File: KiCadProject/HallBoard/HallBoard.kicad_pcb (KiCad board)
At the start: 2 copper layers, 6 parts, among them J101 JST_SM04B, J102 JST_SM04B, U101 TLE493D

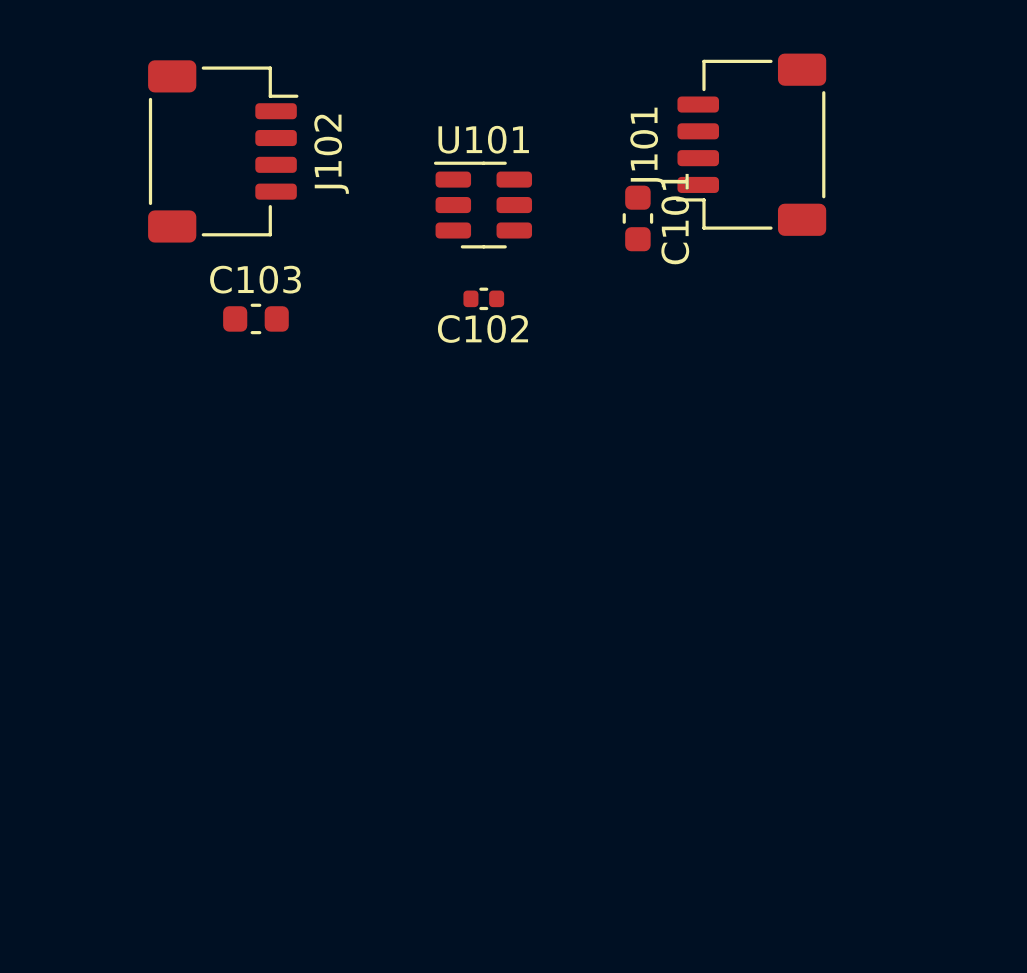
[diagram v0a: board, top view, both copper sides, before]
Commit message: All PCB's should be done. Do a final check before ordering.
Signed-off-by: Eldalote.Electronics <Eldalote.Electronics@gmail.com>
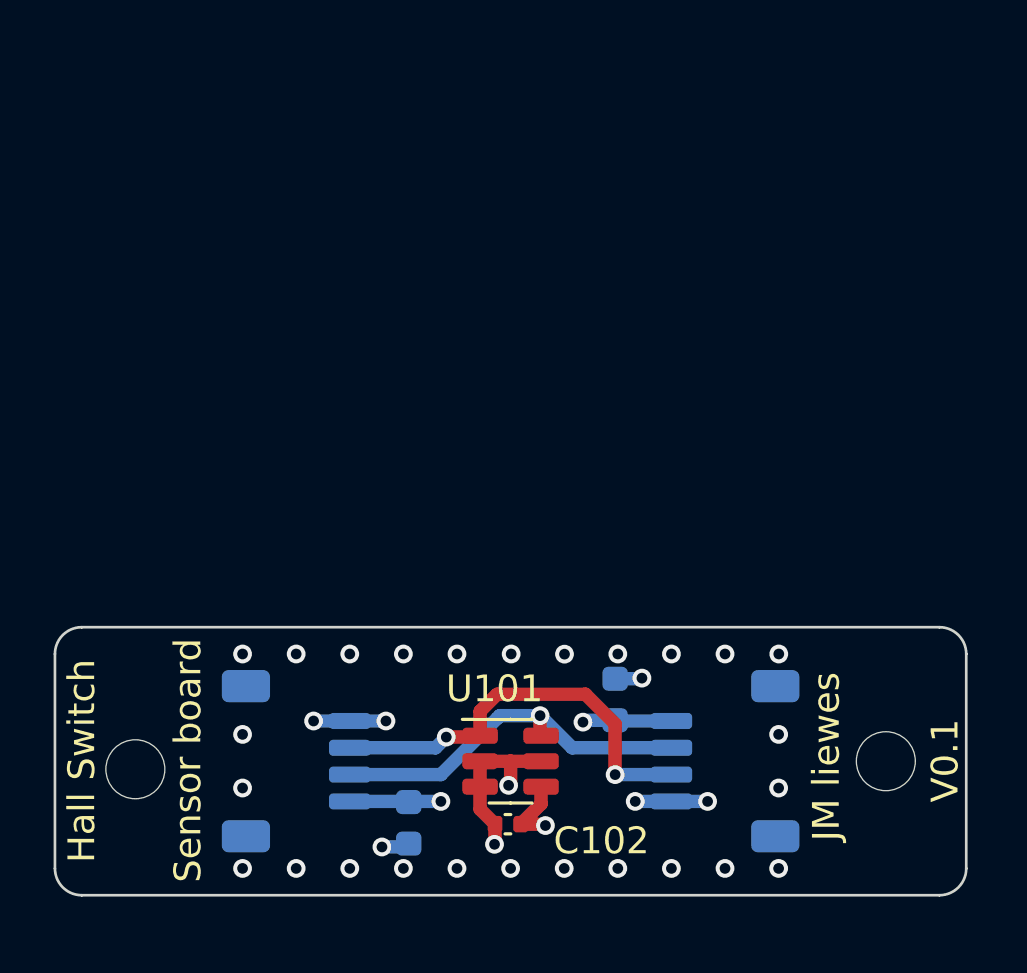
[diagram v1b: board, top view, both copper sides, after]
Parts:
- added REF**: MountingHole_2.2mm_M2, MountingHole:MountingHole_2.2mm_M2, F.Cu at (164.0, 100.0)
- added REF**: MountingHole_2.2mm_M2, MountingHole:MountingHole_2.2mm_M2, F.Cu at (136.0, 100.3)
- C101, C103, J101, J102: moved to B.Cu
- moved C101 24.1 mm to (146.2, 102.3)
- moved J101 23.0 mm to (158.0, 100.0), turned to -90 degrees
- moved J102 22.9 mm to (142.0, 100.0), turned to 90 degrees
- moved U101 20.8 mm to (150.0, 100.0)
- moved C102 19.6 mm to (149.9, 102.3)
- moved C103 19.5 mm to (153.9, 97.7), turned to 90 degrees
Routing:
- net /I2C_SCL: track 0.00 -> 15.7 mm, vias 0 -> 2
- net /I2C_SDA: track 0.00 -> 14.2 mm, vias 0 -> 1
- net GND: track 0.00 -> 14.0 mm, vias 0 -> 34
- net +3V3: track 0.00 -> 9.19 mm, vias 0 -> 3
- added copper zone on In2.Cu, net +3V3
- added copper zone on In1.Cu, net GND
- added copper zone on In3.Cu, net GND
- added copper zone on In4.Cu, net GND
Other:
- board outline added: 34 x 10 mm
- copper layers 2 -> 6
- board text added: "Hall Switch"
- board text added: "JM liewes"
- board text added: "Sensor board"
- board text added: "V0.1"
- board text added: "jlcjlcjlcjlc"

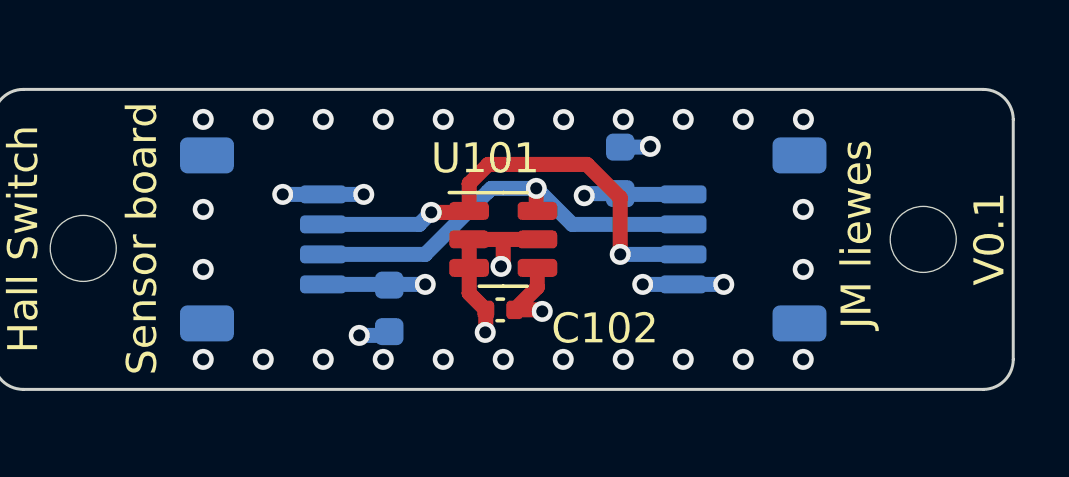
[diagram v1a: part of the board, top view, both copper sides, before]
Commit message: Made ready to order PCBs. Some problems with ordering due to misunderstanding. Thinking about solutions
Signed-off-by: Eldalote.Electronics <Eldalote.Electronics@gmail.com>
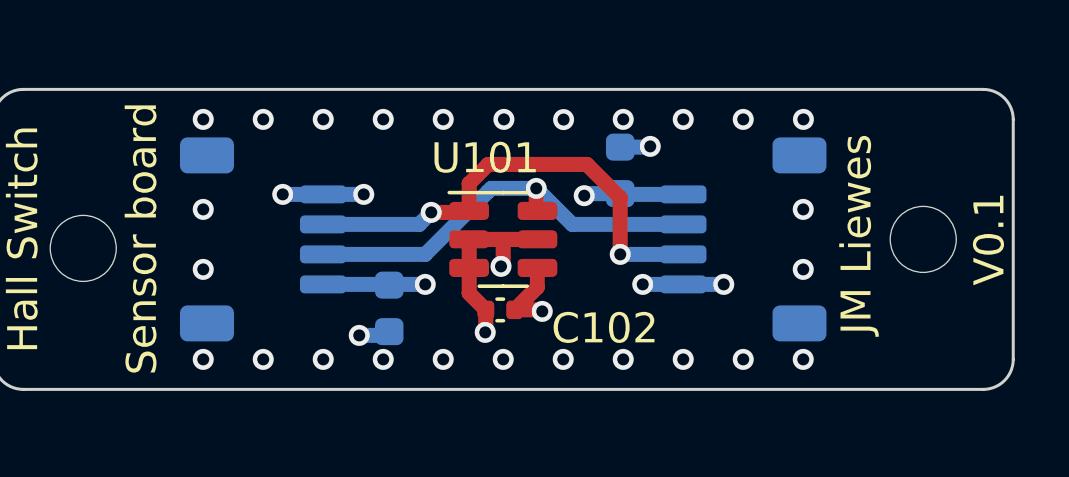
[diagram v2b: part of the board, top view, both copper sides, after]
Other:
- board text added: "JM Liewes"
- board text removed: "JM liewes"
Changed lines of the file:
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@@
       (layerselection 0x00010fc_ffffffff)
       (disableapertmacros false)
-      (usegerberextensions false)
+      (usegerberextensions true)
       (usegerberattributes true)
       (usegerberadvancedattributes true)
@@
       (plotinvisibletext false)
       (sketchpadsonfab false)
-      (subtractmaskfromsilk false)
+      (subtractmaskfromsilk true)
       (outputformat 1)
       (mirror false)
-      (drillshape 1)
+      (drillshape 0)
       (scaleselection 1)
-      (outputdirectory "")
+      (outputdirectory "Fab/")
     )
   )
@@
     (pad "4" smd roundrect (at 1.5 2 90) (size 0.6 1.55) (layers "B.Cu" "B.Paste" "B.Mask") (roundrect_rratio 0.25)
       (net 2 "GND") (pinfunction "Pin_4") (pintype "passive"))
-    (pad "MP" smd roundrect (at -2.8 -1.875 90) (size 1.2 1.8) (layers "B.Cu" "B.Paste" "B.Mask") (roundrect_rratio 0.208333))
-    (pad "MP" smd roundrect (at 2.8 -1.875 90) (size 1.2 1.8) (layers "B.Cu" "B.Paste" "B.Mask") (roundrect_rratio 0.208333))
+    (pad "MP" smd roundrect (at -2.8 -1.875 90) (size 1.2 1.8) (layers "B.Cu" "B.Paste" "B.Mask") (roundrect_rratio 0.2083333333))
+    (pad "MP" smd roundrect (at 2.8 -1.875 90) (size 1.2 1.8) (layers "B.Cu" "B.Paste" "B.Mask") (roundrect_rratio 0.2083333333))
     (model "F:/Engineering/Projects/Divelamp/KiCadImports/3DModels/SM04B-SRSS-TB.STEP"
       (offset (xyz 0 1.5 -0.25))
@@
     (pad "4" smd roundrect (at 1.5 2 270) (size 0.6 1.55) (layers "B.Cu" "B.Paste" "B.Mask") (roundrect_rratio 0.25)
       (net 2 "GND") (pinfunction "Pin_4") (pintype "passive"))
-    (pad "MP" smd roundrect (at -2.8 -1.875 270) (size 1.2 1.8) (layers "B.Cu" "B.Paste" "B.Mask") (roundrect_rratio 0.208333))
-    (pad "MP" smd roundrect (at 2.8 -1.875 270) (size 1.2 1.8) (layers "B.Cu" "B.Paste" "B.Mask") (roundrect_rratio 0.208333))
+    (pad "MP" smd roundrect (at -2.8 -1.875 270) (size 1.2 1.8) (layers "B.Cu" "B.Paste" "B.Mask") (roundrect_rratio 0.2083333333))
+    (pad "MP" smd roundrect (at 2.8 -1.875 270) (size 1.2 1.8) (layers "B.Cu" "B.Paste" "B.Mask") (roundrect_rratio 0.2083333333))
     (model "F:/Engineering/Projects/Divelamp/KiCadImports/3DModels/SM04B-SRSS-TB.STEP"
       (offset (xyz 0 1.5 -0.25))
@@
     (effects (font (size 1 1) (thickness 0.15)) (justify mirror))
   )
-  (gr_text "JM liewes" (at 161.78 99.83 90) (layer "F.SilkS")
+  (gr_text "JM Liewes" (at 161.78 99.83 90) (layer "F.SilkS")
     (effects (font (size 1 1) (thickness 0.16)))
   )

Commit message: Started work on body 3d work
Signed-off-by: Eldalote.Electronics <Eldalote.Electronics@gmail.com>
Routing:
- net +3V3: track 9.19 -> 18.9 mm, vias 3 -> 2
- added copper zone on B.Cu, net GND
- added copper zone on F.Cu, net GND
- removed copper zone on In2.Cu, net +3V3
- removed copper zone on In1.Cu, net GND
- removed copper zone on In3.Cu, net GND
- removed copper zone on In4.Cu, net GND
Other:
- copper layers 6 -> 2
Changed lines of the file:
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@@
   (layers
     (0 "F.Cu" signal)
-    (1 "In1.Cu" signal)
-    (2 "In2.Cu" signal)
-    (3 "In3.Cu" signal)
-    (4 "In4.Cu" signal)
     (31 "B.Cu" signal)
     (32 "B.Adhes" user "B.Adhesive")
@@
       (layer "F.Mask" (type "Top Solder Mask") (thickness 0.01))
       (layer "F.Cu" (type "copper") (thickness 0.035))
-      (layer "dielectric 1" (type "core") (thickness 0.274) (material "FR4") (epsilon_r 4.5) (loss_tangent 0.02))
-      (layer "In1.Cu" (type "copper") (thickness 0.035))
-      (layer "dielectric 2" (type "prepreg") (thickness 0.274) (material "FR4") (epsilon_r 4.5) (loss_tangent 0.02))
-      (layer "In2.Cu" (type "copper") (thickness 0.035))
-      (layer "dielectric 3" (type "core") (thickness 0.274) (material "FR4") (epsilon_r 4.5) (loss_tangent 0.02))
-      (layer "In3.Cu" (type "copper") (thickness 0.035))
-      (layer "dielectric 4" (type "prepreg") (thickness 0.274) (material "FR4") (epsilon_r 4.5) (loss_tangent 0.02))
-      (layer "In4.Cu" (type "copper") (thickness 0.035))
-      (layer "dielectric 5" (type "core") (thickness 0.274) (material "FR4") (epsilon_r 4.5) (loss_tangent 0.02))
+      (layer "dielectric 1" (type "core") (thickness 1.51) (material "FR4") (epsilon_r 4.5) (loss_tangent 0.02))
       (layer "B.Cu" (type "copper") (thickness 0.035))
       (layer "B.Mask" (type "Bottom Solder Mask") (thickness 0.01))
@@
     (effects (font (size 1 1) (thickness 0.15)))
   )
-  (segment (start 150.38 102.35) (end 151.25 102.35) (width 0.5) (layer "F.Cu") (net 1))
-  (segment (start 151.1375 101.5925) (end 150.38 102.35) (width 0.5) (layer "F.Cu") (net 1))
-  (segment (start 151.1375 100.95) (end 151.1375 101.5925) (width 0.5) (layer "F.Cu") (net 1))
-  (segment (start 151.25 102.35) (end 151.3 102.4) (width 0.5) (layer "F.Cu") (net 1))
+  (segment (start 148.2 103.2) (end 150 103.2) (width 0.5) (layer "F.Cu") (net 1))
+  (segment (start 151.85 102.35) (end 150.85 102.35) (width 0.5) (layer "F.Cu") (net 1))
+  (segment (start 150 103.2) (end 150.85 102.35) (width 0.5) (layer "F.Cu") (net 1))
+  (segment (start 150.4 102.33) (end 150.38 102.35) (width 0.5) (layer "F.Cu") (net 1))
+  (segment (start 152.7 101.5) (end 151.85 102.35) (width 0.5) (layer "F.Cu") (net 1))
+  (segment (start 150.38 102.35) (end 150.85 102.35) (width 0.5) (layer "F.Cu") (net 1))
+  (segment (start 147.4 102.4) (end 148.2 103.2) (width 0.5) (layer "F.Cu") (net 1))
+  (segment (start 151.1375 100.95) (end 150.4 101.6875) (width 0.5) (layer "F.Cu") (net 1))
+  (segment (start 147.4 101.5) (end 147.4 102.4) (width 0.5) (layer "F.Cu") (net 1))
+  (segment (start 152.7 98.542453) (end 152.7 101.5) (width 0.5) (layer "F.Cu") (net 1))
+  (segment (start 150.4 101.6875) (end 150.4 102.33) (width 0.5) (layer "F.Cu") (net 1))
   (via (at 147.4 101.5) (size 0.7) (drill 0.4) (layers "F.Cu" "B.Cu") (net 1))
   (via (at 152.7 98.542453) (size 0.7) (drill 0.4) (layers "F.Cu" "B.Cu") (net 1))
-  (via (at 151.3 102.4) (size 0.7) (drill 0.4) (layers "F.Cu" "B.Cu") (net 1))
   (segment (start 152.767453 98.475) (end 153.9 98.475) (width 0.5) (layer "B.Cu") (net 1))
   (segment (start 152.7 98.542453) (end 152.767453 98.475) (width 0.5) (layer "B.Cu") (net 1))
@@
   (segment (start 147.4 101.5) (end 146.25 101.5) (width 0.5) (layer "B.Cu") (net 1))
   (segment (start 148.8625 100) (end 148.8625 100.95) (width 0.5) (layer "F.Cu") (net 2))
+  (segment (start 149.37 102.4) (end 149.42 102.35) (width 0.5) (layer "F.Cu") (net 2))
   (segment (start 148.8625 100) (end 150 100) (width 0.5) (layer "F.Cu") (net 2))
   (segment (start 148.8625 101.7925) (end 149.42 102.35) (width 0.5) (layer "F.Cu") (net 2))
   (segment (start 148.8625 100.95) (end 148.8625 101.7925) (width 0.5) (layer "F.Cu") (net 2))
-  (segment (start 149.42 103.08) (end 149.4 103.1) (width 0.5) (layer "F.Cu") (net 2))
+  (segment (start 148.6 102.4) (end 149.37 102.4) (width 0.5) (layer "F.Cu") (net 2))
   (segment (start 150 100.8255) (end 149.9255 100.9) (width 0.5) (layer "F.Cu") (net 2))
   (segment (start 150 100) (end 151.1375 100) (width 0.5) (layer "F.Cu") (net 2))
   (segment (start 150 100) (end 150 100.8255) (width 0.5) (layer "F.Cu") (net 2))
-  (segment (start 149.42 102.35) (end 149.42 103.08) (width 0.5) (layer "F.Cu") (net 2))
   (via (at 140 101) (size 0.7) (drill 0.4) (layers "F.Cu" "B.Cu") (net 2))
   (via (at 145.2 103.2) (size 0.7) (drill 0.4) (layers "F.Cu" "B.Cu") (net 2))
@@
   (via (at 156 104) (size 0.7) (drill 0.4) (layers "F.Cu" "B.Cu") (net 2))
   (via (at 140 99) (size 0.7) (drill 0.4) (layers "F.Cu" "B.Cu") (net 2))
-  (via (at 149.4 103.1) (size 0.7) (drill 0.4) (layers "F.Cu" "B.Cu") (net 2))
+  (via (at 148.6 102.4) (size 0.7) (drill 0.4) (layers "F.Cu" "B.Cu") (net 2))
   (via (at 152 104) (size 0.7) (drill 0.4) (layers "F.Cu" "B.Cu") (net 2))
   (via (at 152.010917 96.005981) (size 0.7) (drill 0.4) (layers "F.Cu" "B.Cu") (net 2))
@@
   (segment (start 153.9 100.5) (end 156 100.5) (width 0.5) (layer "B.Cu") (net 4))
   (segment (start 144 99.5) (end 147.2 99.5) (width 0.5) (layer "B.Cu") (net 4))
-  (zone (net 2) (net_name "GND") (layers "In1.Cu" "In3.Cu" "In4.Cu") (hatch edge 0.508)
+  (zone (net 2) (net_name "GND") (layers F&B.Cu) (hatch edge 0.508)
     (connect_pads yes (clearance 0.2))
     (min_thickness 0.2) (filled_areas_thickness no)
@@
     (polygon
       (pts
-        (xy 161 106)
-        (xy 139 106)
-        (xy 139 94)
-        (xy 161 94)
+        (xy 161 104.5)
+        (xy 139 104.5)
+        (xy 139 95.5)
+        (xy 161 95.5)
       )
     )
-  )
-  (zone (net 1) (net_name "+3V3") (layer "In2.Cu") (hatch edge 0.508)
-    (connect_pads yes (clearance 0.2))
-    (min_thickness 0.2) (filled_areas_thickness no)
-    (fill yes (thermal_gap 0.508) (thermal_bridge_width 0.508))
-    (polygon
-      (pts
-        (xy 158 103)
-        (xy 142 103)
-        (xy 142 97)
-        (xy 158 97)
-      )
-    )
